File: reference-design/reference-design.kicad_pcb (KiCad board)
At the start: 2 copper layers, 70 x 42 mm, 21 parts

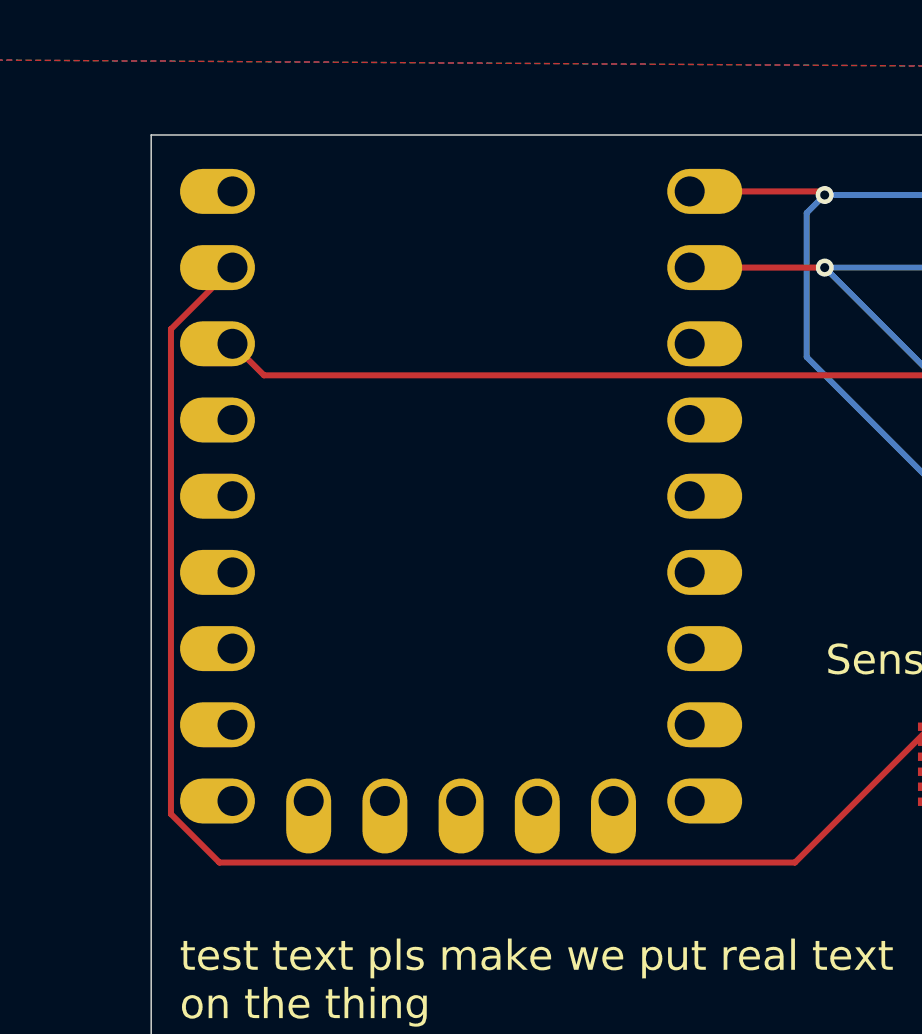
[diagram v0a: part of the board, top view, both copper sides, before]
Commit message: changed MCU footprint
Replaced throughhole MCU footprint with SMD one
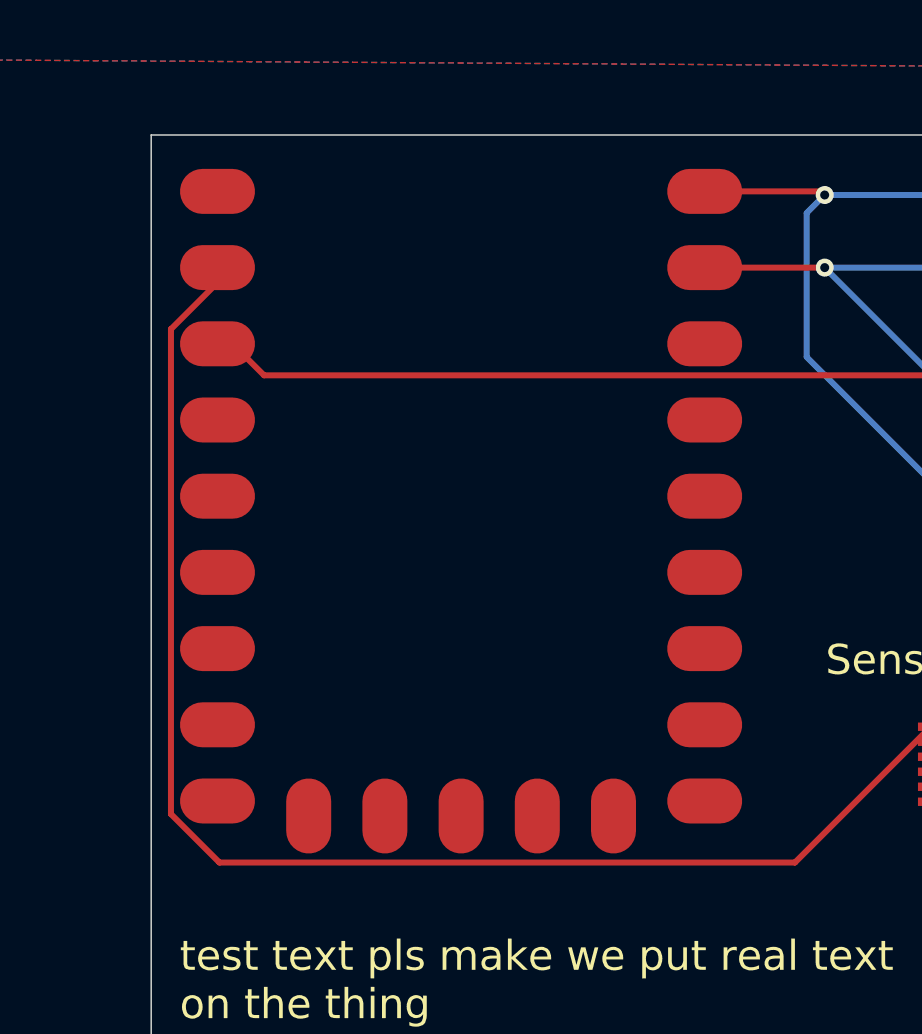
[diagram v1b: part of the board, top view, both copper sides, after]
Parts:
- MCU1: footprint RP2040-Zero:rp2040-zero-tht -> RP2040-Zero:rp2040-zero-smd
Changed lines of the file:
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@@
 			(psa4output no)
 			(plot_black_and_white yes)
-			(plotinvisibletext no)
 			(sketchpadsonfab no)
 			(plotpadnumbers no)
@@
 		)
 	)
-	(footprint "RP2040-Zero:rp2040-zero-tht"
+	(footprint "RP2040-Zero:rp2040-zero-smd"
 		(layer "F.Cu")
 		(at 22.88 24.54)
@@
 		(sheetname "/")
 		(sheetfile "reference-design.kicad_sch")
-		(attr through_hole exclude_from_pos_files)
+		(attr smd exclude_from_pos_files)
 		(fp_rect
 			(start -9 -11.75)
@@
 			(layer "Dwgs.User")
 		)
-		(pad "1" thru_hole oval
+		(pad "1" smd oval
 			(at 7.62 -10.16 180)
 			(size 2.5 1.5)
-			(drill 1
+			(drill
 				(offset -0.5 0)
 			)
-			(layers "*.Cu" "*.Mask")
-			(remove_unused_layers no)
+			(layers "F.Cu" "F.Mask" "F.Paste")
 			(net 4 "i2c0_sda")
 			(pinfunction "0")
 			(pintype "bidirectional")
 		)
-		(pad "2" thru_hole oval
+		(pad "2" smd oval
 			(at 7.62 -7.62 180)
 			(size 2.5 1.5)
-			(drill 1
+			(drill
 				(offset -0.5 0)
 			)
-			(layers "*.Cu" "*.Mask")
-			(remove_unused_layers no)
+			(layers "F.Cu" "F.Mask" "F.Paste")
 			(net 3 "i2c0_scl")
 			(pinfunction "1")
 			(pintype "bidirectional")
 		)
-		(pad "3" thru_hole oval
+		(pad "3" smd oval
 			(at 7.62 -5.08 180)
 			(size 2.5 1.5)
-			(drill 1
+			(drill
 				(offset -0.5 0)
 			)
-			(layers "*.Cu" "*.Mask")
-			(remove_unused_layers no)
+			(layers "F.Cu" "F.Mask" "F.Paste")
 			(net 33 "unconnected-(MCU1-2-Pad3)")
 			(pinfunction "2")
 			(pintype "bidirectional+no_connect")
 		)
-		(pad "4" thru_hole oval
+		(pad "4" smd oval
 			(at 7.62 -2.54 180)
 			(size 2.5 1.5)
-			(drill 1
+			(drill
 				(offset -0.5 0)
 			)
-			(layers "*.Cu" "*.Mask")
-			(remove_unused_layers no)
+			(layers "F.Cu" "F.Mask" "F.Paste")
 			(net 35 "unconnected-(MCU1-3-Pad4)")
 			(pinfunction "3")
 			(pintype "bidirectional+no_connect")
 		)
-		(pad "5" thru_hole oval
+		(pad "5" smd oval
 			(at 7.62 0 180)
 			(size 2.5 1.5)
-			(drill 1
+			(drill
 				(offset -0.5 0)
 			)
-			(layers "*.Cu" "*.Mask")
-			(remove_unused_layers no)
+			(layers "F.Cu" "F.Mask" "F.Paste")
 			(net 25 "unconnected-(MCU1-4-Pad5)")
 			(pinfunction "4")
 			(pintype "bidirectional+no_connect")
 		)
-		(pad "6" thru_hole oval
+		(pad "6" smd oval
 			(at 7.62 2.54 180)
 			(size 2.5 1.5)
-			(drill 1
+			(drill
 				(offset -0.5 0)
 			)
-			(layers "*.Cu" "*.Mask")
-			(remove_unused_layers no)
+			(layers "F.Cu" "F.Mask" "F.Paste")
 			(net 23 "unconnected-(MCU1-5-Pad6)")
 			(pinfunction "5")
 			(pintype "bidirectional+no_connect")
 		)
-		(pad "7" thru_hole oval
+		(pad "7" smd oval
 			(at 7.62 5.08 180)
 			(size 2.5 1.5)
-			(drill 1
+			(drill
 				(offset -0.5 0)
 			)
-			(layers "*.Cu" "*.Mask")
-			(remove_unused_layers no)
+			(layers "F.Cu" "F.Mask" "F.Paste")
 			(net 37 "unconnected-(MCU1-6-Pad7)")
 			(pinfunction "6")
 			(pintype "bidirectional+no_connect")
 		)
-		(pad "8" thru_hole oval
+		(pad "8" smd oval
 			(at 7.62 7.62 180)
 			(size 2.5 1.5)
-			(drill 1
+			(drill
 				(offset -0.5 0)
 			)
-			(layers "*.Cu" "*.Mask")
-			(remove_unused_layers no)
+			(layers "F.Cu" "F.Mask" "F.Paste")
 			(net 27 "unconnected-(MCU1-7-Pad8)")
 			(pinfunction "7")
 			(pintype "bidirectional+no_connect")
 		)
-		(pad "9" thru_hole oval
+		(pad "9" smd oval
 			(at 7.62 10.16 180)
 			(size 2.5 1.5)
-			(drill 1
+			(drill
 				(offset -0.5 0)
 			)
-			(layers "*.Cu" "*.Mask")
-			(remove_unused_layers no)
+			(layers "F.Cu" "F.Mask" "F.Paste")
 			(net 30 "unconnected-(MCU1-8-Pad9)")
 			(pinfunction "8")
 			(pintype "bidirectional+no_connect")
 		)
-		(pad "10" thru_hole oval
+		(pad "10" smd oval
 			(at 5.08 10.16 90)
 			(size 2.5 1.5)
-			(drill 1
+			(drill
 				(offset -0.5 0)
 			)
-			(layers "*.Cu" "*.Mask")
-			(remove_unused_layers no)
+			(layers "F.Cu" "F.Mask" "F.Paste")
 			(net 36 "unconnected-(MCU1-9-Pad10)")
 			(pinfunction "9")
 			(pintype "bidirectional+no_connect")
 		)
-		(pad "11" thru_hole oval
+		(pad "11" smd oval
 			(at 2.54 10.16 90)
 			(size 2.5 1.5)
-			(drill 1
+			(drill
 				(offset -0.5 0)
 			)
-			(layers "*.Cu" "*.Mask")
-			(remove_unused_layers no)
+			(layers "F.Cu" "F.Mask" "F.Paste")
 			(net 26 "unconnected-(MCU1-10-Pad11)")
 			(pinfunction "10")
 			(pintype "bidirectional+no_connect")
 		)
-		(pad "12" thru_hole oval
+		(pad "12" smd oval
 			(at 0 10.16 90)
 			(size 2.5 1.5)
-			(drill 1
+			(drill
 				(offset -0.5 0)
 			)
-			(layers "*.Cu" "*.Mask")
-			(remove_unused_layers no)
+			(layers "F.Cu" "F.Mask" "F.Paste")
 			(net 34 "unconnected-(MCU1-11-Pad12)")
 			(pinfunction "11")
 			(pintype "bidirectional+no_connect")
 		)
-		(pad "13" thru_hole oval
+		(pad "13" smd oval
 			(at -2.54 10.16 90)
 			(size 2.5 1.5)
-			(drill 1
+			(drill
 				(offset -0.5 0)
 			)
-			(layers "*.Cu" "*.Mask")
-			(remove_unused_layers no)
+			(layers "F.Cu" "F.Mask" "F.Paste")
 			(net 28 "unconnected-(MCU1-12-Pad13)")
 			(pinfunction "12")
 			(pintype "bidirectional+no_connect")
 		)
-		(pad "14" thru_hole oval
+		(pad "14" smd oval
 			(at -5.08 10.16 90)
 			(size 2.5 1.5)
-			(drill 1
+			(drill
 				(offset -0.5 0)
 			)
-			(layers "*.Cu" "*.Mask")
-			(remove_unused_layers no)
+			(layers "F.Cu" "F.Mask" "F.Paste")
 			(net 29 "unconnected-(MCU1-13-Pad14)")
 			(pinfunction "13")
 			(pintype "bidirectional+no_connect")
 		)
-		(pad "15" thru_hole oval
+		(pad "15" smd oval
 			(at -7.62 10.16)
 			(size 2.5 1.5)
-			(drill 1
+			(drill
 				(offset -0.5 0)
 			)
-			(layers "*.Cu" "*.Mask")
-			(remove_unused_layers no)
+			(layers "F.Cu" "F.Mask" "F.Paste")
 			(net 24 "unconnected-(MCU1-14-Pad15)")
 			(pinfunction "14")
 			(pintype "bidirectional+no_connect")
 		)
-		(pad "16" thru_hole oval
+		(pad "16" smd oval
 			(at -7.62 7.62)
 			(size 2.5 1.5)
-			(drill 1
+			(drill
 				(offset -0.5 0)
 			)
-			(layers "*.Cu" "*.Mask")
-			(remove_unused_layers no)
+			(layers "F.Cu" "F.Mask" "F.Paste")
 			(net 31 "unconnected-(MCU1-15-Pad16)")
 			(pinfunction "15")
 			(pintype "bidirectional+no_connect")
 		)
-		(pad "17" thru_hole oval
+		(pad "17" smd oval
 			(at -7.62 5.08)
 			(size 2.5 1.5)
-			(drill 1
+			(drill
 				(offset -0.5 0)
 			)
-			(layers "*.Cu" "*.Mask")
-			(remove_unused_layers no)
+			(layers "F.Cu" "F.Mask" "F.Paste")
 			(net 21 "unconnected-(MCU1-26-Pad17)")
 			(pinfunction "26")
 			(pintype "bidirectional+no_connect")
 		)
-		(pad "18" thru_hole oval
+		(pad "18" smd oval
 			(at -7.62 2.54)
 			(size 2.5 1.5)
-			(drill 1
+			(drill
 				(offset -0.5 0)
 			)
-			(layers "*.Cu" "*.Mask")
-			(remove_unused_layers no)
+			(layers "F.Cu" "F.Mask" "F.Paste")
 			(net 20 "unconnected-(MCU1-27-Pad18)")
 			(pinfunction "27")
 			(pintype "bidirectional+no_connect")
 		)
-		(pad "19" thru_hole oval
+		(pad "19" smd oval
 			(at -7.62 0)
 			(size 2.5 1.5)
-			(drill 1
+			(drill
 				(offset -0.5 0)
 			)
-			(layers "*.Cu" "*.Mask")
-			(remove_unused_layers no)
+			(layers "F.Cu" "F.Mask" "F.Paste")
 			(net 32 "unconnected-(MCU1-28-Pad19)")
 			(pinfunction "28")
 			(pintype "bidirectional+no_connect")
 		)
-		(pad "20" thru_hole oval
+		(pad "20" smd oval
 			(at -7.62 -2.54)
 			(size 2.5 1.5)
-			(drill 1
+			(drill
 				(offset -0.5 0)
 			)
-			(layers "*.Cu" "*.Mask")
-			(remove_unused_layers no)
+			(layers "F.Cu" "F.Mask" "F.Paste")
 			(net 22 "unconnected-(MCU1-29-Pad20)")
 			(pinfunction "29")
 			(pintype "bidirectional+no_connect")
 		)
-		(pad "21" thru_hole oval
+		(pad "21" smd oval
 			(at -7.62 -5.08)
 			(size 2.5 1.5)
-			(drill 1
+			(drill
 				(offset -0.5 0)
 			)
-			(layers "*.Cu" "*.Mask")
-			(remove_unused_layers no)
+			(layers "F.Cu" "F.Mask" "F.Paste")
 			(net 8 "+3.3V")
 			(pinfunction "3V3")
 			(pintype "power_out")
 		)
-		(pad "22" thru_hole oval
+		(pad "22" smd oval
 			(at -7.62 -7.62)
 			(size 2.5 1.5)
-			(drill 1
+			(drill
 				(offset -0.5 0)
 			)
-			(layers "*.Cu" "*.Mask")
-			(remove_unused_layers no)
+			(layers "F.Cu" "F.Mask" "F.Paste")
 			(net 1 "GND")
 			(pinfunction "GND")
 			(pintype "power_out")
 		)
-		(pad "23" thru_hole oval
+		(pad "23" smd oval
 			(at -7.62 -10.16)
 			(size 2.5 1.5)
-			(drill 1
+			(drill
 				(offset -0.5 0)
 			)
-			(layers "*.Cu" "*.Mask")
-			(remove_unused_layers no)
+			(layers "F.Cu" "F.Mask" "F.Paste")
 			(net 17 "+5V")
 			(pinfunction "5V")
@@
 		)
 		(embedded_fonts no)
-		(model "${KIPRJMOD}/components/RP2040-Zero/RP2040-Zero.step"
-			(offset
-				(xyz 0 0 0)
-			)
-			(scale
-				(xyz 1 1 1)
-			)
-			(rotate
-				(xyz 0 0 0)
-			)
-		)
 	)
 	(footprint "AH49FNTR_G1:SC59_DIO"

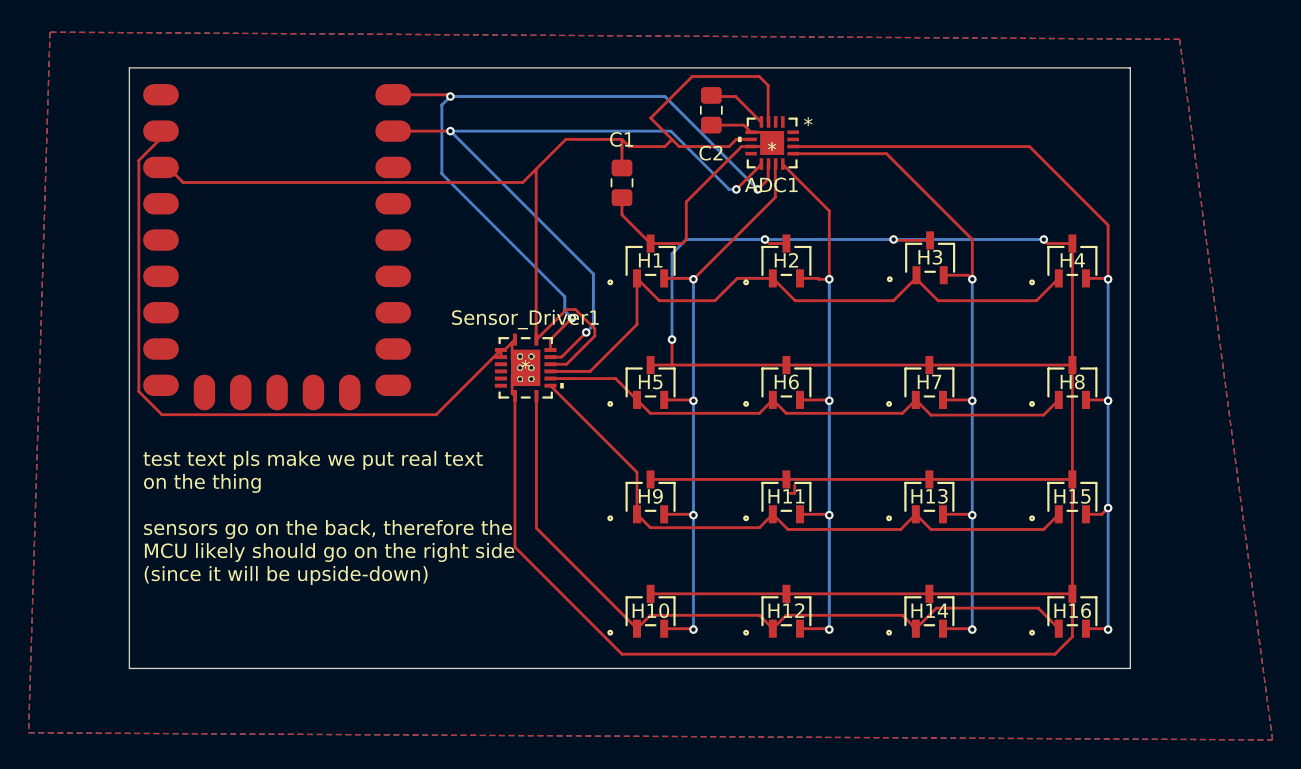
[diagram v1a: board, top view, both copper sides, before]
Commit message: test autorouting, pretty cool stuff
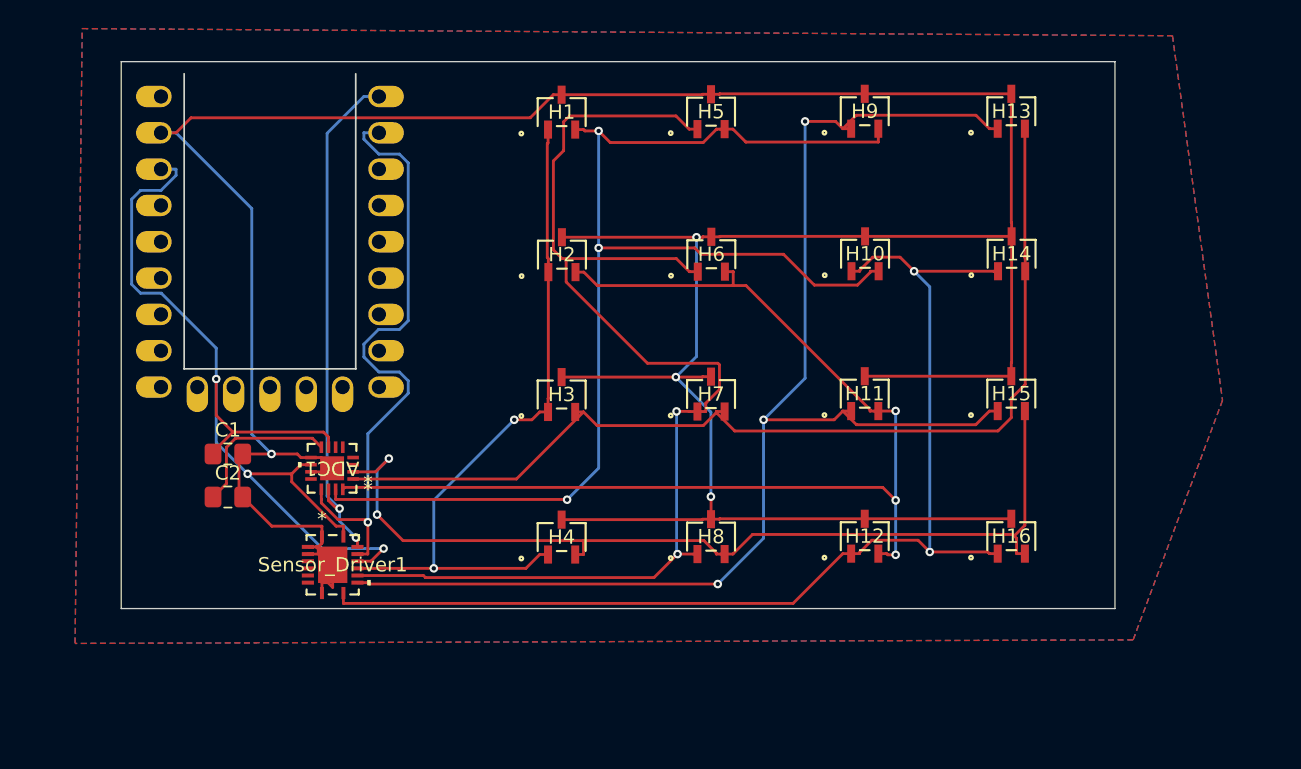
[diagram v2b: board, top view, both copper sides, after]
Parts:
- MCU1: footprint RP2040-Zero:rp2040-zero-smd -> RP2040-Zero:rp2040-zero-tht
- moved C2 43.3 mm to (19.4, 42.5), turned to 0 degrees
- moved H4 40.6 mm to (42.8, 45.3)
- moved ADC1 38.3 mm to (26.7, 40.5)
- moved C1 33.5 mm to (19.4, 39.5), turned to 0 degrees
- moved H9 30.8 mm to (64.0, 15.5)
- moved H10 29.2 mm to (64.0, 25.5)
- moved H13 27.6 mm to (74.2, 15.5)
- moved H3 27.5 mm to (42.8, 35.3)
- moved H8 27.5 mm to (53.2, 45.3)
- moved H14 25.7 mm to (74.2, 25.5)
- moved H5 19.4 mm to (53.2, 15.6)
- moved Sensor_Driver1 19.3 mm to (26.8, 47.2)
- moved H2 15.7 mm to (42.8, 25.6)
- moved H7 15.3 mm to (53.2, 35.3)
- moved H1 12.1 mm to (42.8, 15.6)
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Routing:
- net row2: track 43.5 -> 93.2 mm, vias 0 -> 3
- net row1: track 38.6 -> 84.9 mm, vias 0 -> 2
- net GND: track 283.9 -> 237.9 mm
- net col0: track 43.2 -> 88.0 mm, vias 4 -> 3
- net col1: track 42.3 -> 78.4 mm, vias 4 -> 3
- net row3: track 51.4 -> 79.9 mm, vias 0 -> 2
- net col2: track 50.7 -> 71.5 mm, vias 4 -> 0
- net i2c0_sda: track 53.2 -> 36.3 mm, vias 3 -> 2
- net +3.3V: track 81.5 -> 67.3 mm, vias 0 -> 3
- net col3: track 59.1 -> 66.0 mm, vias 4 -> 2
- net i2c0_scl: track 50.3 -> 43.6 mm, vias 3 -> 1
- net Net-(ADC1-DECAP): track 4.46 -> 11.0 mm
- net row0: track 44.0 -> 48.9 mm, vias 0 -> 2
- net (no net): track 0.88 -> 0.00 mm
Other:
- board size 70 x 42 mm -> 69.5 x 38.2 mm
- board text removed: "test text pls make we put real text on the thing sensors go on the back, therefore the MCU likely should go on the right side (since it will be upside-down)"
